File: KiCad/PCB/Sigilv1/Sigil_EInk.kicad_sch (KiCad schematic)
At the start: 13 parts, among them J2 INLAND E-PAPER HEADER (8-PIN), J3 BUZZER 2-PIN HEADER, J4 ANALOG JOYSTICK HEADER (5-PIN), J5 STATUS RING CABLE (JST-XH 3), J6 FRONT LIGHT CABLE (JST-XH 3), U1 REMOVABLE ESP32 DEVKIT / 2 x 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, U2 74AHCT1G125, U3 74AHCT1G125

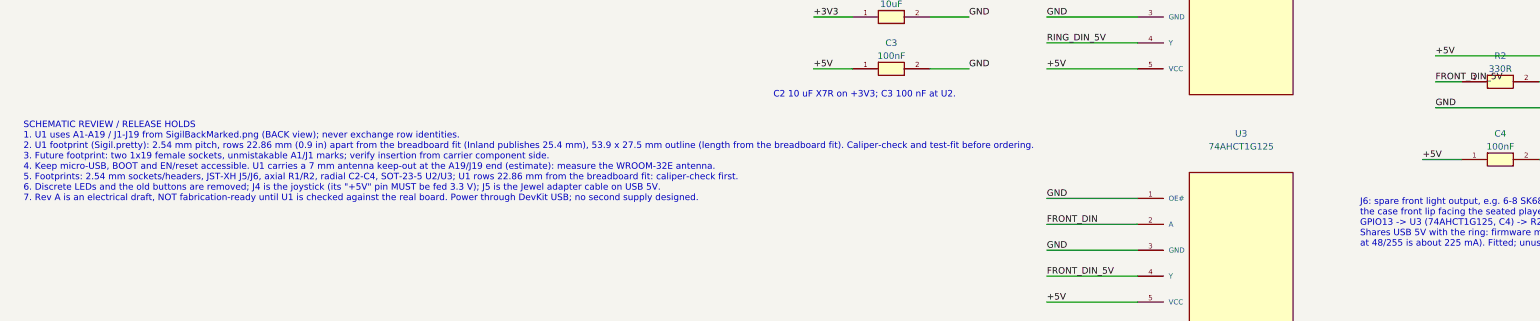
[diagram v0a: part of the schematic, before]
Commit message: Sigil E-ink PCB: measured DevKit footprint, routed board, fab outputs
- U1 footprint rows 22.225 mm (7/8 in) apart per owner measurement,
  25.4 x 53.975 mm outline; renamed ESP32_DevKit_38_Socket_Row22.225mm.
- Antenna keep-out narrowed to the measured antenna (6.35 x 19.05 mm)
  so the pin rows stay routable.
- Board top edge moved up 0.5 mm to clear silkscreen.
- Routed with Freerouting v2.4.1 plus a hand-placed BUZZER track; GND
  pours on both layers with solid pad connections. KiCad 10.0.6 DRC:
  0 violations, 0 unconnected, 0 schematic parity issues.
- Added BOM CSV, Gerber/drill zip and position CSV under fab/.
- Not fabrication-verified: U1 row spacing still needs a test-fit.

Co-Authored-By: Claude Opus 5.5 <noreply@anthropic.com>
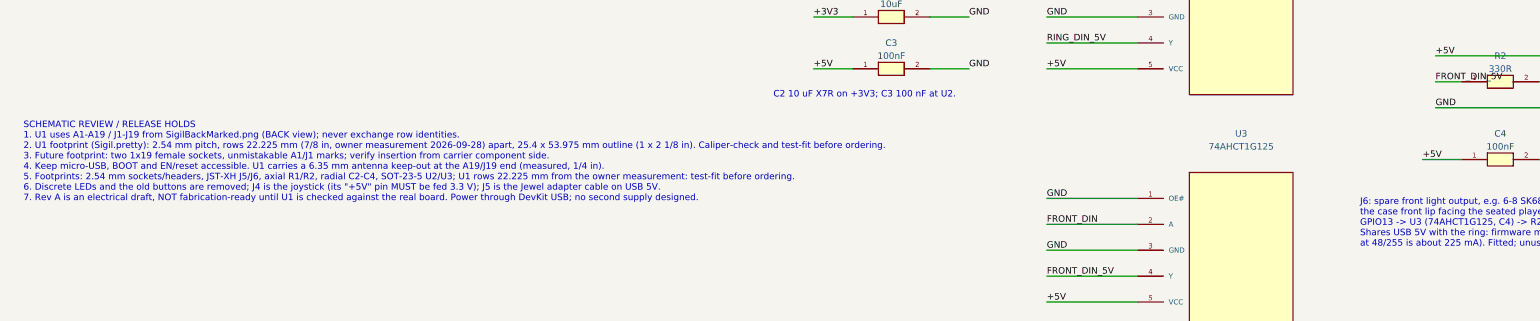
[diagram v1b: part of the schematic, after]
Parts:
- U1: footprint Sigil:ESP32_DevKit_38_Socket_Row22.86mm -> Sigil:ESP32_DevKit_38_Socket_Row22.225mm
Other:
- note added: "SCHEMATIC REVIEW / RELEASE HOLDS 1. U1 uses A1-A19 / J1-J19 from SigilBackMarked.png (BACK view); never exchange row identities. 2. U1 footprint (Sigil.pretty): 2.54 mm pitch, rows 22.225 mm (7/8 in, owner measurement 2026-09-28) apart, 25.4 x 53.975 mm outline (1 x 2 1/8 in). Caliper-check and test-fit before ordering. 3. Future footprint: two 1x19 female sockets, unmistakable A1/J1 marks; verif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"
- note removed: "SCHEMATIC REVIEW / RELEASE HOLDS 1. U1 uses A1-A19 / J1-J19 from SigilBackMarked.png (BACK view); never exchange row identities. 2. U1 footprint (Sigil.pretty): 2.54 mm pitch, rows 22.86 mm (0.9 in) apart from the breadboard fit (Inland publishes 25.4 mm), 53.9 x 27.5 mm outline (length from the breadboard fit). Caliper-check and test-fit before ordering. 3. Future footprint: two 1x19 female sock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"
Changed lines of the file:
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@@
 		)
 	)
-	(text "SCHEMATIC REVIEW / RELEASE HOLDS\n1. U1 uses A1-A19 / J1-J19 from SigilBackMarked.png (BACK view); never exchange row identities.\n2. U1 footprint (Sigil.pretty): 2.54 mm pitch, rows 22.86 mm (0.9 in) apart from the breadboard fit (Inland publishes 25.4 mm), 53.9 x 27.5 mm outline (length from the breadboard fit). Caliper-check and test-fit before ordering.\n3. Future footprint: two 1x19 female sockets, unmistakable A1/J1 marks; verify insertion from carrier component side.\n4. Keep micro-USB, BOOT and EN/reset accessible. U1 carries a 7 mm antenna keep-out at the A19/J19 end (estimate): measure the WROOM-32E antenna.\n5. Footprints: 2.54 mm sockets/headers, JST-XH J5/J6, axial R1/R2, radial C2-C4, SOT-23-5 U2/U3; U1 rows 22.86 mm from the breadboard fit: caliper-check first.\n6. Discrete LEDs and the old buttons are removed; J4 is the joystick (its \"+5V\" pin MUST be fed 3.3 V); J5 is the Jewel adapter cable on USB 5V.\n7. Rev A is an electrical draft, NOT fabrication-ready until U1 is checked against the real board. Power through DevKit USB; no second supply designed."
+	(text "SCHEMATIC REVIEW / RELEASE HOLDS\n1. U1 uses A1-A19 / J1-J19 from SigilBackMarked.png (BACK view); never exchange row identities.\n2. U1 footprint (Sigil.pretty): 2.54 mm pitch, rows 22.225 mm (7/8 in, owner measurement 2026-09-28) apart, 25.4 x 53.975 mm outline (1 x 2 1/8 in). Caliper-check and test-fit before ordering.\n3. Future footprint: two 1x19 female sockets, unmistakable A1/J1 marks; verify insertion from carrier component side.\n4. Keep micro-USB, BOOT and EN/reset accessible. U1 carries a 6.35 mm antenna keep-out at the A19/J19 end (measured, 1/4 in).\n5. Footprints: 2.54 mm sockets/headers, JST-XH J5/J6, axial R1/R2, radial C2-C4, SOT-23-5 U2/U3; U1 rows 22.225 mm from the owner measurement: test-fit before ordering.\n6. Discrete LEDs and the old buttons are removed; J4 is the joystick (its \"+5V\" pin MUST be fed 3.3 V); J5 is the Jewel adapter cable on USB 5V.\n7. Rev A is an electrical draft, NOT fabrication-ready until U1 is checked against the real board. Power through DevKit USB; no second supply designed."
 		(exclude_from_sim no)
 		(at 28 211 0)
@@
 			)
 		)
-		(property "Footprint" "Sigil:ESP32_DevKit_38_Socket_Row22.86mm"
+		(property "Footprint" "Sigil:ESP32_DevKit_38_Socket_Row22.225mm"
 			(at 88.9 101.6 0)
 			(hide yes)

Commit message: KiCad: Sigil_OLED draws the joystick J4 like the E-ink; SW1-SW5 removed
The OLED Sigil uses the same thumbstick on the same GPIOs (34/35/32) since
2026-10-01, so build_schematic.py gives it J4 and drops the pushbutton
symbol, footprint and drawing; verify_schematic.py checks the joystick rows
on both drafts. KiCad 10 CLI ERC: 0 violations on all three schematics;
verify_schematic.py passes; E-ink PCB DRC and schematic parity still clean
(its schematic changed only in note text). README, hardware reference and
STAGED_CHANGES updated.

Co-Authored-By: Claude Opus 5.5 <noreply@anthropic.com>
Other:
- note added: "Unmarked 5-pin analog thumbstick; pins in module order. "+5V" pin is fed 3.3 V: VRX/VRY swing to the supply and the ESP32 ADC must not see 5 V. SW is a switch to GND (internal pull-up). Directions + click are the five menu keys (on-screen compass). Axis direction depends on mounting; firmware can swap/invert. Firmware: Sigil PlatformIO envs sigil and sigil-oled."
- note removed: "Unmarked 5-pin analog thumbstick; pins in module order. "+5V" pin is fed 3.3 V: VRX/VRY swing to the supply and the ESP32 ADC must not see 5 V. SW is a switch to GND (internal pull-up). Directions + click are the five menu keys (on-screen compass). Axis direction depends on mounting; firmware can swap/invert. Firmware: Sigil PlatformIO env sigil (E-ink build)."
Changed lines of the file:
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@@
+		)
+	)
+	(text "SCHEMATIC REVIEW / RELEASE HOLDS\n1. U1 uses A1-A19 / J1-J19 from SigilBackMarked.png (BACK view); never exchange row identities.\n2. U1 footprint (Sigil.pretty): 2.54 mm pitch, rows 22.225 mm (7/8 in, owner measurement 2026-09-28) apart, 25.4 x 53.975 mm outline (1 x 2 1/8 in). Caliper-check and test-fit before ordering.\n3. Future footprint: two 1x19 female sockets, unmistakable A1/J1 marks; verify insertion from carrier component side.\n4. Keep micro-USB, BOOT and EN/reset accessible. U1 carries a 6.35 mm antenna keep-out at the A19/J19 end (measured, 1/4 in).\n5. Footprints: 2.54 mm sockets/headers, JST-XH J5/J6, axial R1/R2, radial C2-C4, SOT-23-5 U2/U3; U1 rows 22.225 mm from the owner measurement: test-fit before ordering.\n6. Discrete LEDs and the old buttons are removed; J4 is the joystick (its \"+5V\" pin MUST be fed 3.3 V); J5 is the Jewel adapter cable on USB 5V.\n7. Rev A is an electrical draft, NOT fabrication-ready until U1 is checked against the real board. Power through DevKit USB; no second supply designed."
+		(exclude_from_sim no)
+		(at 28 211 0)
+		(effects
+			(font
+				(size 1.27 1.27)
+			)
+			(justify left top)
 		)
 	)
@@
 		)
 	)
+	(text "Unmarked 5-pin analog thumbstick; pins in module order.\n\"+5V\" pin is fed 3.3 V: VRX/VRY swing to the supply and the\nESP32 ADC must not see 5 V. SW is a switch to GND (internal pull-up).\nDirections + click are the five menu keys (on-screen compass).\nAxis direction depends on mounting; firmware can swap/invert.\nFirmware: Sigil PlatformIO envs sigil and sigil-oled."
+		(exclude_from_sim no)
+		(at 290 86.36 0)
+		(effects
+			(font
+				(size 1.27 1.27)
+			)
+			(justify left top)
+		)
+	)
 	(text "J6: spare front light output, e.g. 6-8 SK6812 RGBW pixels on\nthe case front lip facing the seated player. Own data line:\nGPIO13 -> U3 (74AHCT1G125, C4) -> R2 (330 ohm) -> DIN; pinout as J5.\nShares USB 5V with the ring: firmware must cap both (7 + 8 pixels\nat 48/255 is about 225 mA). Fitted; unused until a strip is added."
 		(exclude_from_sim no)
@@
 		)
 	)
-	(text "SCHEMATIC REVIEW / RELEASE HOLDS\n1. U1 uses A1-A19 / J1-J19 from SigilBackMarked.png (BACK view); never exchange row identities.\n2. U1 footprint (Sigil.pretty): 2.54 mm pitch, rows 22.225 mm (7/8 in, owner measurement 2026-09-28) apart, 25.4 x 53.975 mm outline (1 x 2 1/8 in). Caliper-check and test-fit before ordering.\n3. Future footprint: two 1x19 female sockets, unmistakable A1/J1 marks; verify insertion from carrier component side.\n4. Keep micro-USB, BOOT and EN/reset accessible. U1 carries a 6.35 mm antenna keep-out at the A19/J19 end (measured, 1/4 in).\n5. Footprints: 2.54 mm sockets/headers, JST-XH J5/J6, axial R1/R2, radial C2-C4, SOT-23-5 U2/U3; U1 rows 22.225 mm from the owner measurement: test-fit before ordering.\n6. Discrete LEDs and the old buttons are removed; J4 is the joystick (its \"+5V\" pin MUST be fed 3.3 V); J5 is the Jewel adapter cable on USB 5V.\n7. Rev A is an electrical draft, NOT fabrication-ready until U1 is checked against the real board. Power through DevKit USB; no second supply designed."
-		(exclude_from_sim no)
-		(at 28 211 0)
-		(effects
-			(font
-				(size 1.27 1.27)
-			)
-			(justify left top)
-		)
-	)
 	(text "black wire"
 		(exclude_from_sim no)
@@
 			)
 			(justify left top)
-		)
-	)
-	(text "Unmarked 5-pin analog thumbstick; pins in module order.\n\"+5V\" pin is fed 3.3 V: VRX/VRY swing to the supply and the\nESP32 ADC must not see 5 V. SW is a switch to GND (internal pull-up).\nDirections + click are the five menu keys (on-screen compass).\nAxis direction depends on mounting; firmware can swap/invert.\nFirmware: Sigil PlatformIO env sigil (E-ink build)."
-		(exclude_from_sim no)
-		(at 290 86.36 0)
-		(effects
-			(font
-				(size 1.27 1.27)
-			)
-			(justify left top)
